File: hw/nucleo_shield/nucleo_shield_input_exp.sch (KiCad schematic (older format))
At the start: 2 parts, among them U7 PCF8574A, U8 PCF8574A

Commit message: WIP: add more IO
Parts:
- added P14: CONN_IN4, Pin_Headers:Pin_Header_Straight_1x08, symbol CONN_01X08
- added U13, U14: PCF8574A, Housings_DIP:DIP-16__300, symbol PCF8574A
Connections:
- net +3V3: now also U13.1 (A0), U13.16 (VDD), U14.1 (A0), U14.16 (VDD)
- net GND: now also U13.2 (A1), U13.3 (A2), U13.8 (VSS), U14.2 (A1), U14.3 (A2), U14.8 (VSS)
- new net: P14.6 (P6), U13.10 (P5)
- new net: P14.7 (P7), U13.11 (P6)
- new net: P14.8 (P8), U13.12 (P7)
- new net: P14.1 (P1), U13.4 (P0)
- new net: P14.2 (P2), U13.5 (P1)
- new net: P14.3 (P3), U13.6 (P2)
- new net: P14.4 (P4), U13.7 (P3)
- new net: P14.5 (P5), U13.9 (P4)
- new net I2C2_SCL: U13.14 (SCL), U14.14 (SCL)
- new net I2C2_SDA: U13.15 (SDA), U14.15 (SDA)
- new net INT2: U13.13 (~INT~), U14.13 (~INT~)
- new net in17: U14.4 (P0)
- new net in18: U14.5 (P1)
- new net in19: U14.6 (P2)
- new net in20: U14.7 (P3)
- new net in21: U14.9 (P4)
- new net in22: U14.10 (P5)
- new net in23: U14.11 (P6)
- new net in24: U14.12 (P7)
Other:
- moved on the sheet: U7, U8

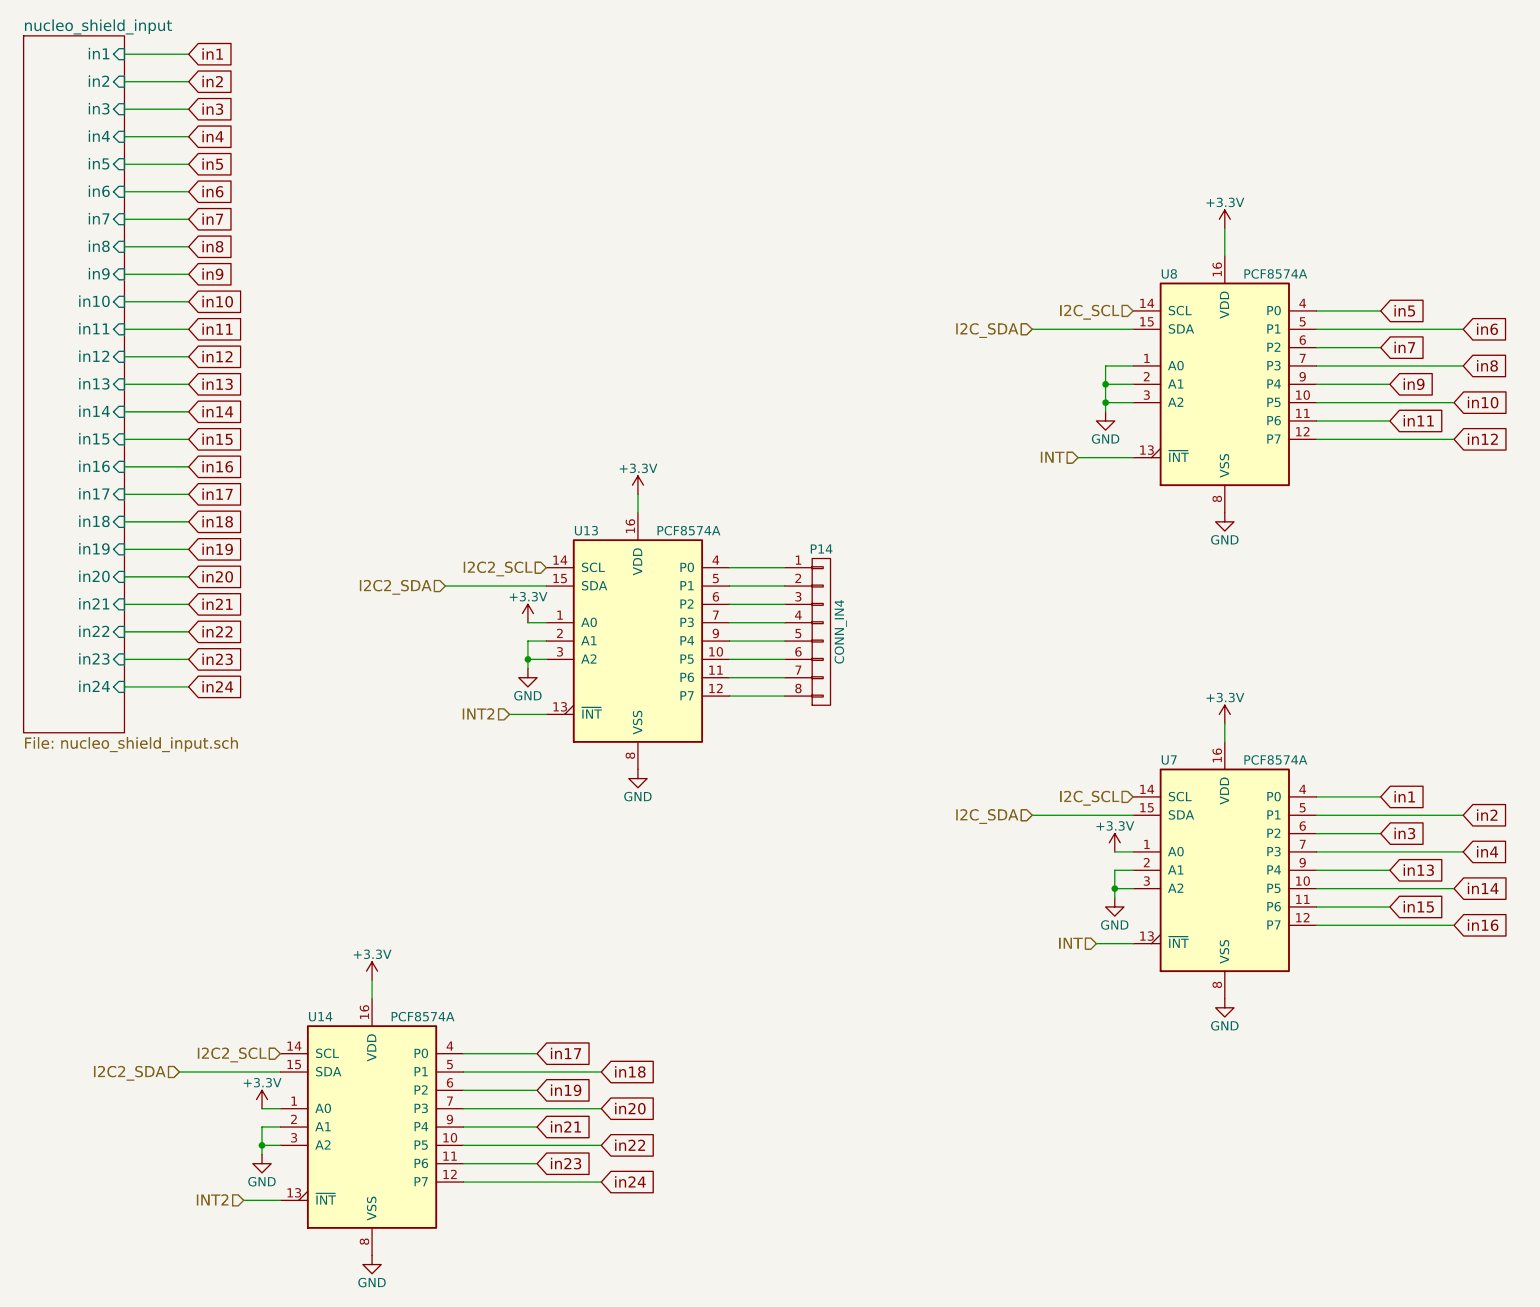
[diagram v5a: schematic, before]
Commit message: HW: rework of nucleo shield to add more IOs
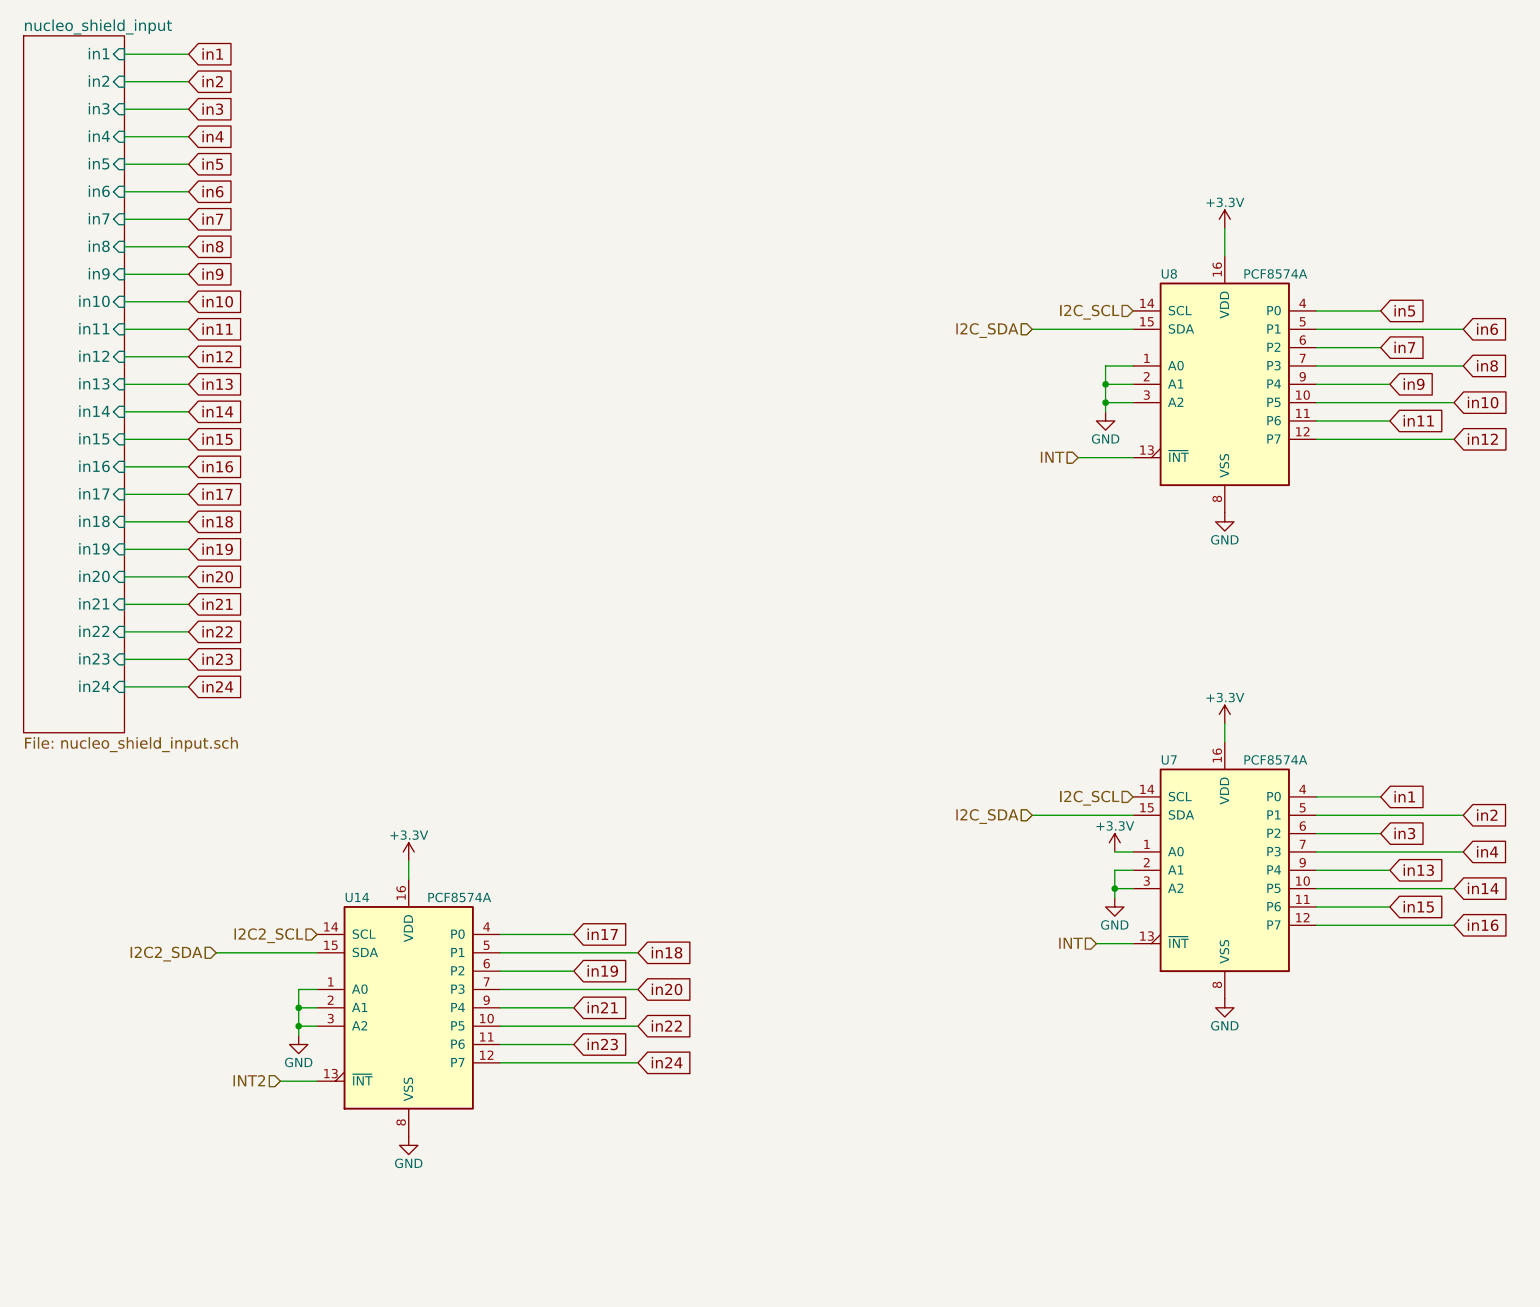
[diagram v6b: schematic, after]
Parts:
- removed P14: CONN_IN4, Pin_Headers:Pin_Header_Straight_1x08, symbol CONN_01X08
- removed U13: PCF8574A, Housings_DIP:DIP-16__300, symbol PCF8574A
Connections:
- net +3V3: no longer U14.1 (A0)
- net GND: now also U14.1 (A0)
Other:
- moved on the sheet: U14
